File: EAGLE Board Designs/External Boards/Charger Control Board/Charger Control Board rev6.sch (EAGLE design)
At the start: 121 parts, among them U1 CPC1002N, U2 CDSOT23-T24CAN-Q

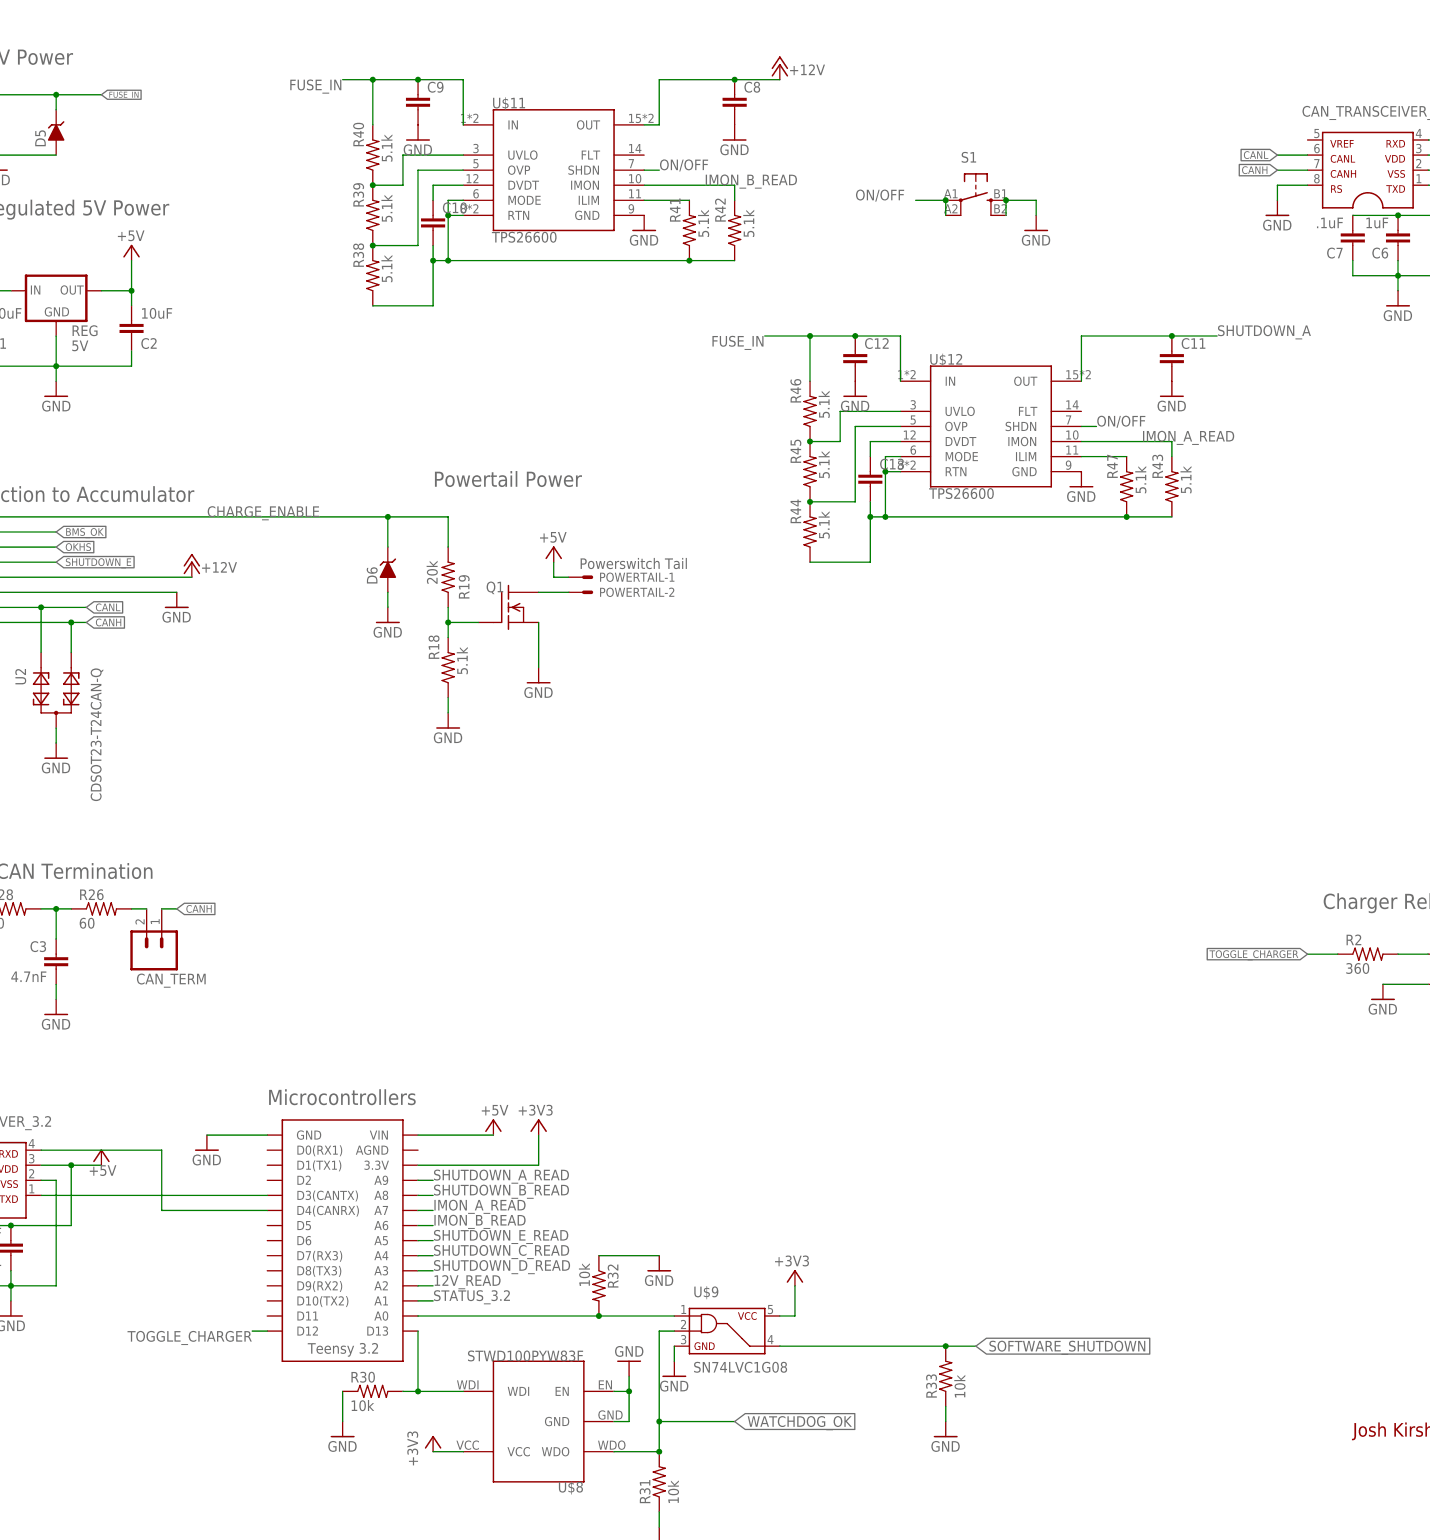
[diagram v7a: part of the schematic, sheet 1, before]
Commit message: Made silk screen look better and made the schematic look better
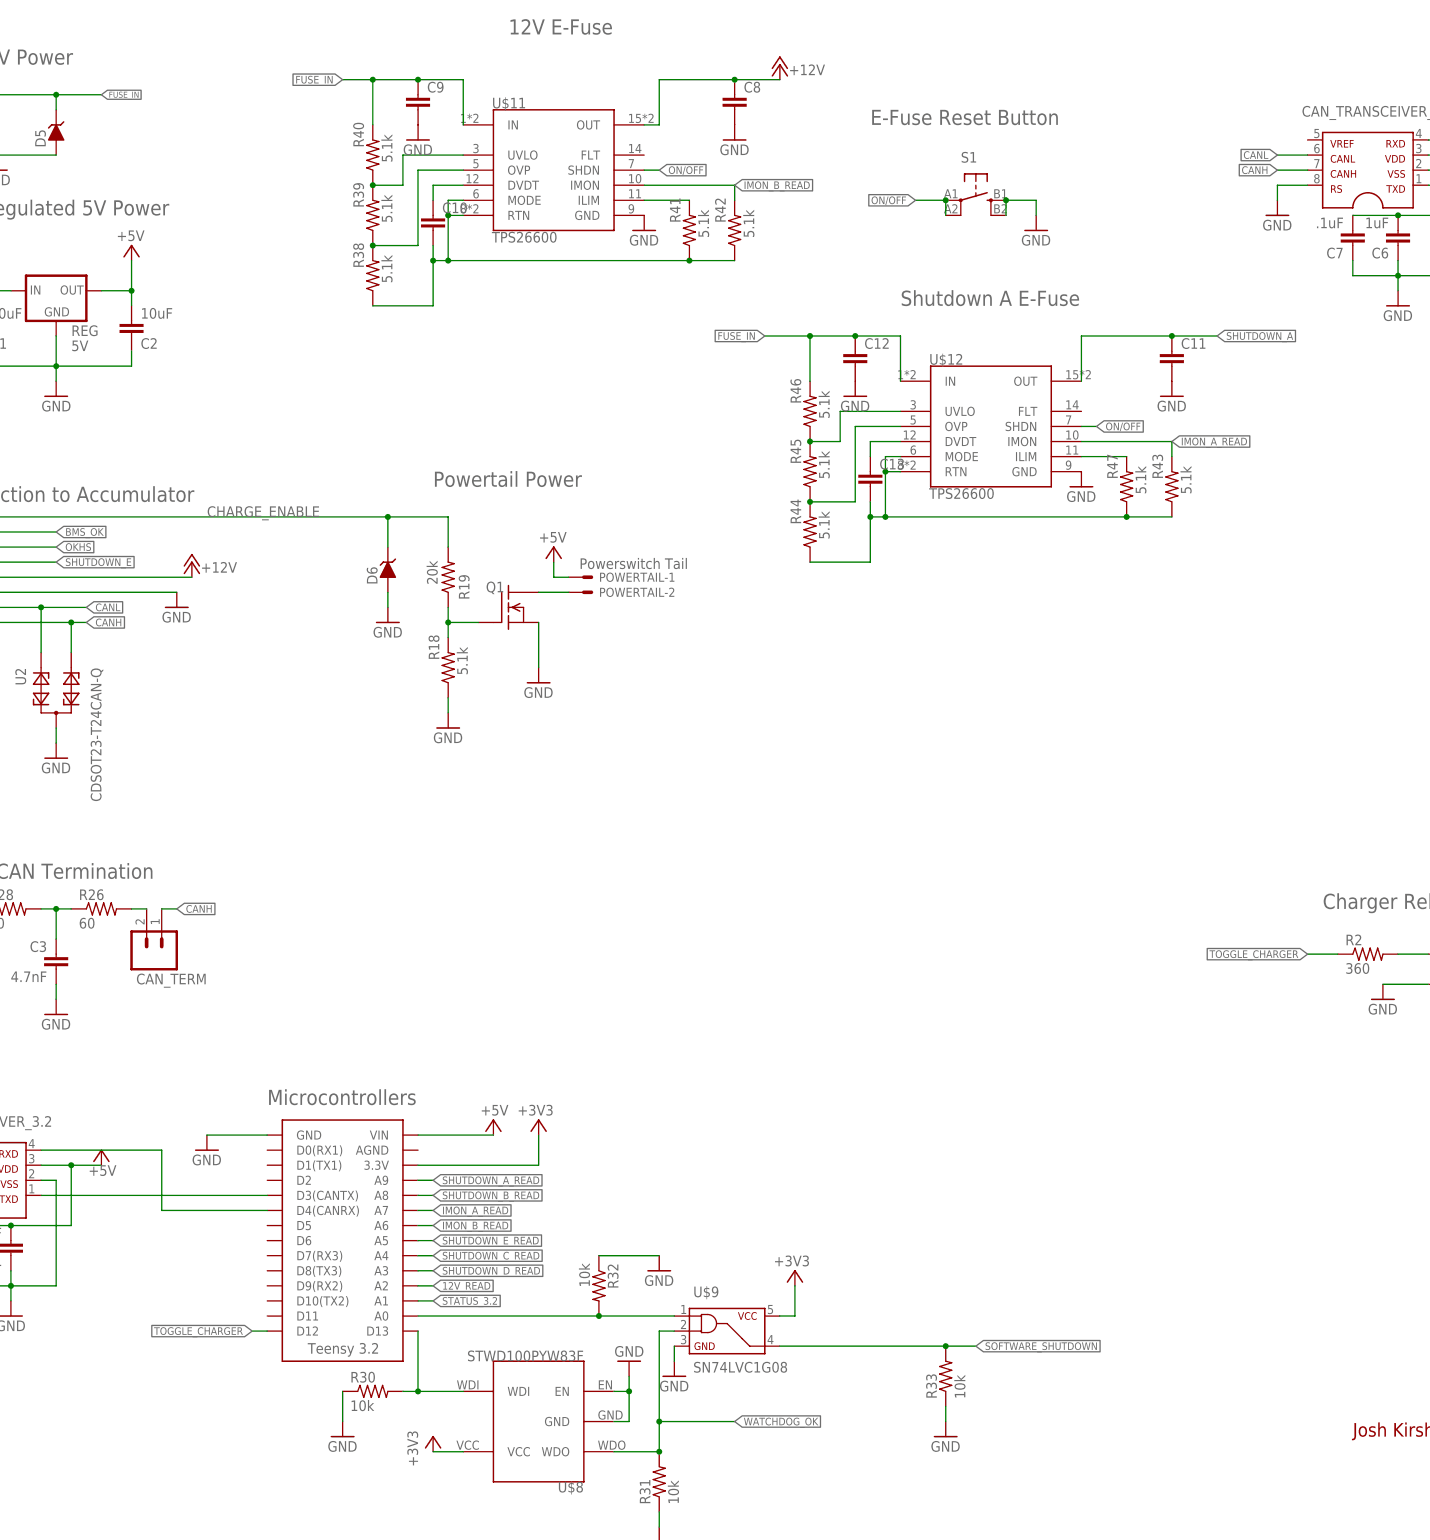
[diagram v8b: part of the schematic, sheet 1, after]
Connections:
- net N$35 renamed RTN_A
- net N$36 renamed OVP_A
- net N$37 renamed UVLO_A
- net N$38 renamed ILIM_A
- net N$39 renamed RTN_B
- net N$41 renamed OVP_B
- net N$44 renamed DVDT_A
- net N$45 renamed UVLO_B
- net N$46 renamed ILIM
- net N$50 renamed DVDT_B
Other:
- note added: "12V E-Fuse"
- note added: "E-Fuse Reset Button"
- note added: "Shutdown A E-Fuse"
